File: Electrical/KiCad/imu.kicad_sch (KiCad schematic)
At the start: 3 parts, among them U6 LSM6DSO32TR

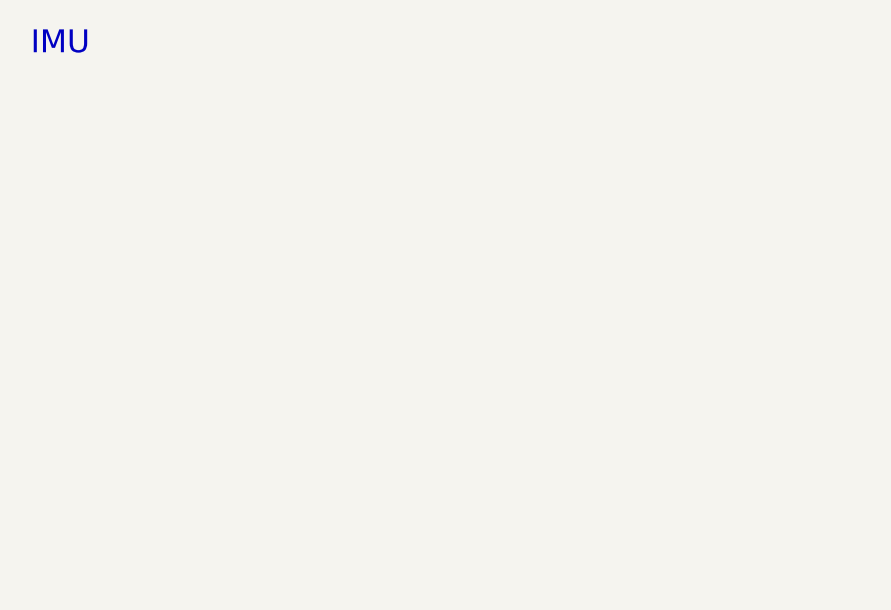
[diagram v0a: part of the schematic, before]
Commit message: Added some labels to the schematic
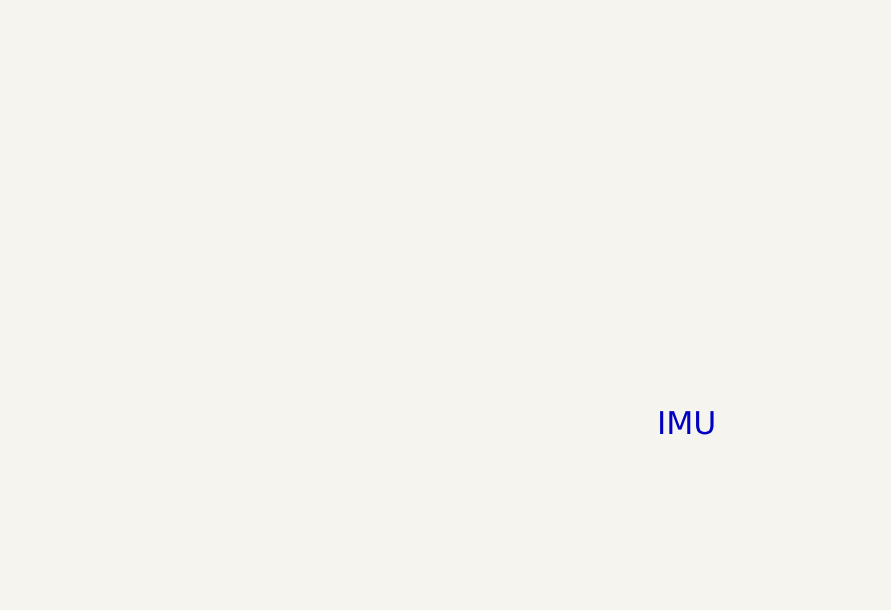
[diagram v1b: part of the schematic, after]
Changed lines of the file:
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@@
 	(text "IMU"
 		(exclude_from_sim no)
-		(at 20.32 18.796 0)
+		(at 89.916 61.214 0)
 		(effects
 			(font
